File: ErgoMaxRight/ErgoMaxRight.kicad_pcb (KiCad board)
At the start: 2 copper layers, 182.8 x 169.2 mm, 103 parts, among them J1 PJ-320A, K1 F12, K10 8 *, K11 7 &, K12 6 ^, K13 KEYSW, K14 KEYSW, K15 P, K16 O, K17 I, K18 U, K19 Y, K2 F11, K20 KEYSW, K21 KEYSW, K22 ; :, K23 L, K24 K, K25 J, K26 H, K27 KEYSW, K28 KEYSW, K29 KEYSW, K3 F10, K30 / ?, K31 . >, K32 , <, K33 M, K34 N, K35 KEYSW, K36 KEYSW, K37 KEYSW, K38 KEYSW, K39 KEYSW, K4 F9, K40 KEYSW, K41 KEYSW, K42 KEYSW, K43 KEYSW, K44 KEYSW, K5 F8, K6 F7, K7 KEYSW, K8 0 ), K9 9 (, U1 ProMicro

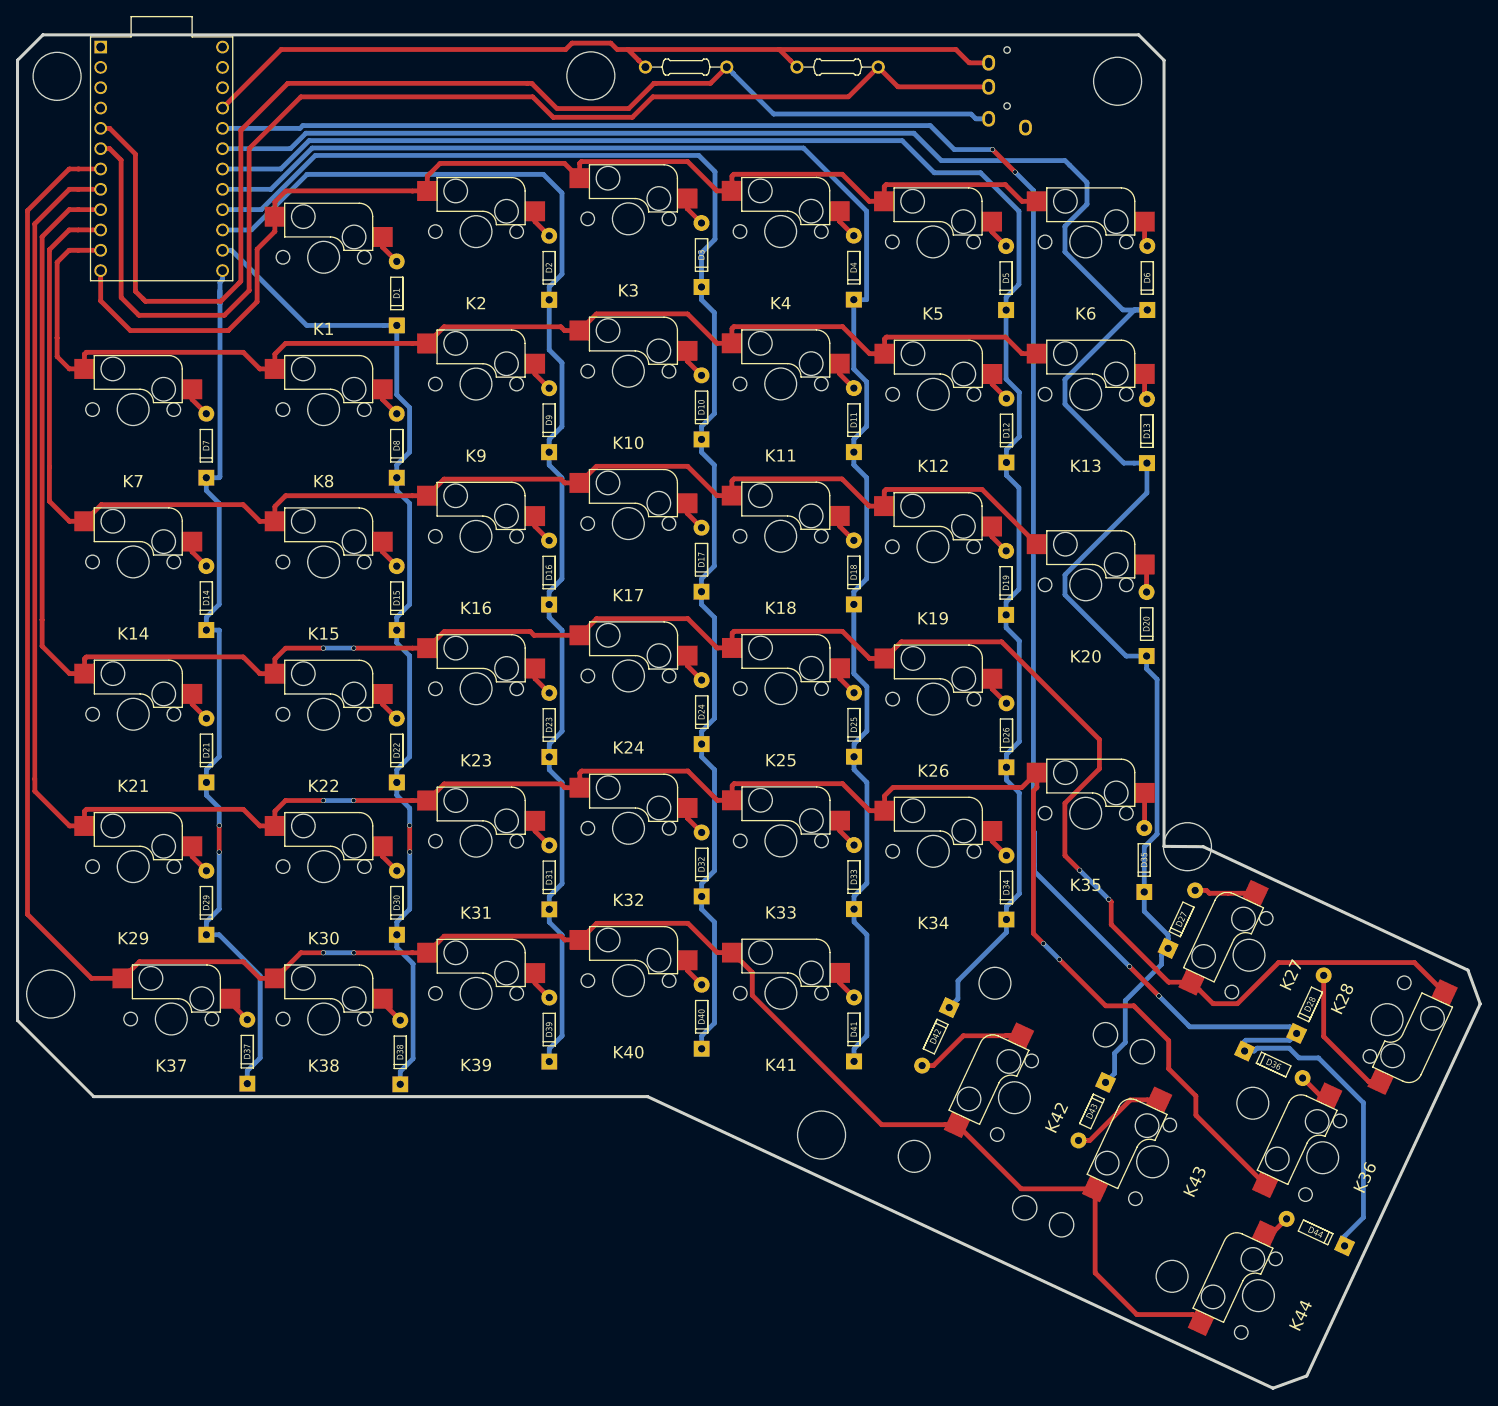
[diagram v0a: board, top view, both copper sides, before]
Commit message: feat: using smd components
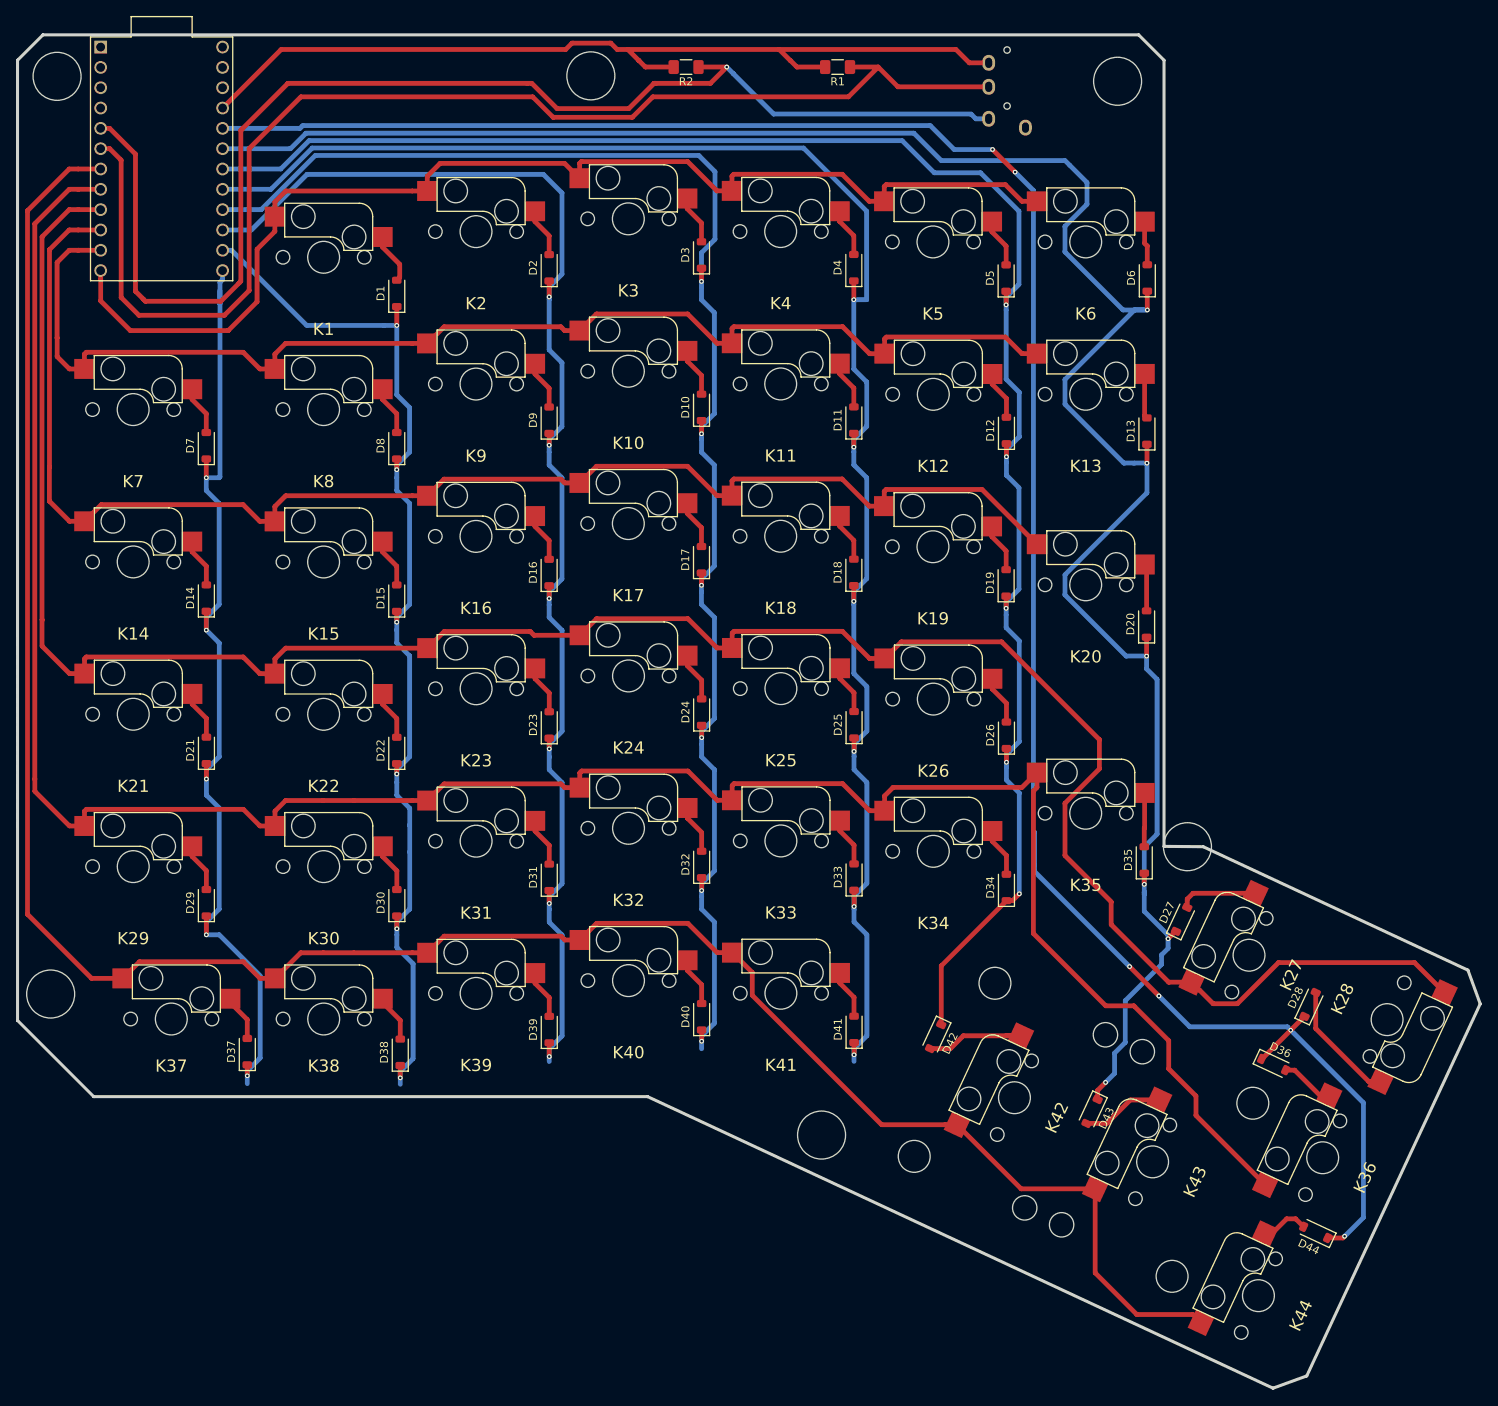
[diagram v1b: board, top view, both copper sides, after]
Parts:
- D1, D10, D11, D12, D13, D14, D15, D16, D17, D18, D19, D2, D20, D21, D22, D23, D24, D25, D26, D27, D28, D29, D3, D30, D31, D32, D33, D34, D35, D36, D37, D38, D39, D4, D40, D41, D42, D43, D44, D5, D6, D7, D8, D9: footprint Keebio-Parts:Diode_Long -> Diode_SMD:D_SOD-123
- R1, R2: footprint Keebio-Parts:Resistor -> Resistor_SMD:R_1206_3216Metric_Pad1.30x1.75mm_HandSolder
- turned D1 to 90 degrees
- turned D10 to 90 degrees
- turned D11 to 90 degrees
- turned D12 to 90 degrees
- turned D13 to 90 degrees
- turned D14 to 90 degrees
- turned D15 to 90 degrees
- turned D16 to 90 degrees
- turned D17 to 90 degrees
- turned D18 to 90 degrees
- turned D19 to 90 degrees
- turned D2 to 90 degrees
- turned D20 to 90 degrees
- turned D21 to 90 degrees
- turned D22 to 90 degrees
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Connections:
- U1 pad 1: Net-(U1-Pad1) -> unconnected-(U1-TX-Pad1)
- U1 pad 2: Net-(U1-Pad2) -> unconnected-(U1-RX-Pad2)
- U1 pad 22: Net-(U1-Pad22) -> unconnected-(U1-RST-Pad22)
- U1 pad 24: Net-(U1-Pad24) -> unconnected-(U1-RAW-Pad24)
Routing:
- net /Col6: track 258.2 -> 270.5 mm, vias 0 -> 6
- net /Col4: track 200.5 -> 211.7 mm, vias 0 -> 6
- net /Col2: track 162.2 -> 171.9 mm, vias 0 -> 6
- net /Col5: track 213.2 -> 222.7 mm, vias 0 -> 5
- net /Col0: track 114.4 -> 123.8 mm, vias 2 -> 5
- net /Col3: track 182.2 -> 191.6 mm, vias 0 -> 6
- net /Col1: track 128.5 -> 136.8 mm, vias 2 -> 6
- net VCC: track 106.4 -> 113.4 mm
- net /Col7: track 276.0 -> 270.6 mm, vias 4 -> 6
- net SCL: track 156.1 -> 159.6 mm
- net SDA: track 158.8 -> 162.3 mm, vias 0 -> 1
- net Net-(D36-A): track 4.23 -> 6.78 mm
- net Net-(D44-A): track 3.48 -> 6.02 mm
- net Net-(D37-A): track 3.51 -> 5.86 mm
- net Net-(D8-A): track 3.80 -> 6.15 mm
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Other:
- copper layers 2 -> 4
- net class Default removed
- rule pad_to_mask_clearance: 0.051 -> 0

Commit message: feat: final version for produccion
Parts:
- moved D35 3.24 mm to (247.9, 139.0)
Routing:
- net /Col6: track 270.5 -> 274.3 mm
- net Net-(D35-A): track 6.75 -> 9.30 mm
- net /Row3: vias 0 -> 2
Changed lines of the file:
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@@
       (plot_on_all_layers_selection 0x0000000_00000000)
       (disableapertmacros false)
-      (usegerberextensions false)
+      (usegerberextensions true)
       (usegerberattributes false)
       (usegerberadvancedattributes false)
@@
       (psa4output false)
       (plotreference true)
-      (plotvalue true)
+      (plotvalue false)
       (plotinvisibletext false)
       (sketchpadsonfab false)
-      (subtractmaskfromsilk false)
+      (subtractmaskfromsilk true)
       (outputformat 1)
       (mirror false)
@@
   )
   (footprint "Diode_SMD:D_SOD-123" (layer "F.Cu")
-    (at 251.18 138.99 90)
+    (at 247.94 138.98 90)
     (descr "SOD-123")
     (tags "SOD-123")
@@
     (fp_line (start 1.6 0.8) (end -1.6 0.8)
       (stroke (width 0.1) (type solid)) (layer "F.Fab"))
-    (pad "1" smd roundrect (at -1.55 0 180) (size 1.3 1.75) (layers "F.Cu" "F.Paste" "F.Mask") (roundrect_rratio 0.192308)
+    (pad "1" smd roundrect (at -1.55 0 180) (size 1.3 1.75) (layers "F.Cu" "F.Paste" "F.Mask") (roundrect_rratio 0.1923076923)
       (net 17 "SCL") (pintype "passive"))
-    (pad "2" smd roundrect (at 1.55 0 180) (size 1.3 1.75) (layers "F.Cu" "F.Paste" "F.Mask") (roundrect_rratio 0.192308)
+    (pad "2" smd roundrect (at 1.55 0 180) (size 1.3 1.75) (layers "F.Cu" "F.Paste" "F.Mask") (roundrect_rratio 0.1923076923)
       (net 15 "VCC") (pintype "passive"))
     (model "${KICAD6_3DMODEL_DIR}/Resistor_SMD.3dshapes/R_1206_3216Metric.wrl"
@@
     (fp_line (start 1.6 0.8) (end -1.6 0.8)
       (stroke (width 0.1) (type solid)) (layer "F.Fab"))
-    (pad "1" smd roundrect (at -1.55 0 180) (size 1.3 1.75) (layers "F.Cu" "F.Paste" "F.Mask") (roundrect_rratio 0.192308)
+    (pad "1" smd roundrect (at -1.55 0 180) (size 1.3 1.75) (layers "F.Cu" "F.Paste" "F.Mask") (roundrect_rratio 0.1923076923)
       (net 16 "SDA") (pintype "passive"))
-    (pad "2" smd roundrect (at 1.55 0 180) (size 1.3 1.75) (layers "F.Cu" "F.Paste" "F.Mask") (roundrect_rratio 0.192308)
+    (pad "2" smd roundrect (at 1.55 0 180) (size 1.3 1.75) (layers "F.Cu" "F.Paste" "F.Mask") (roundrect_rratio 0.1923076923)
       (net 15 "VCC") (pintype "passive"))
     (model "${KICAD6_3DMODEL_DIR}/Resistor_SMD.3dshapes/R_1206_3216Metric.wrl"
@@
   (segment (start 245.35012 167.791762) (end 246.343273 166.798609) (width 0.6) (layer "F.Cu") (net 6))
   (segment (start 251.51334 87.02956) (end 251.51334 89.37956) (width 0.6) (layer "F.Cu") (net 6))
+  (segment (start 247.94 141.21) (end 251.18 144.45) (width 0.6) (layer "F.Cu") (net 6))
   (segment (start 251.55906 67.88558) (end 251.55906 70.23558) (width 0.6) (layer "F.Cu") (net 6))
   (segment (start 251.4727 111.15194) (end 251.4727 113.50194) (width 0.6) (layer "F.Cu") (net 6))
-  (segment (start 251.18 140.64) (end 251.18 142.03) (width 0.6) (layer "F.Cu") (net 6))
   (segment (start 245.35012 168.928432) (end 245.35012 167.791762) (width 0.6) (layer "F.Cu") (net 6))
+  (segment (start 247.94 140.63) (end 247.94 141.21) (width 0.6) (layer "F.Cu") (net 6))
   (segment (start 255.087633 147.911168) (end 254.161187 148.837614) (width 0.6) (layer "F.Cu") (net 6))
   (segment (start 255.15434 147.911168) (end 255.087633 147.911168) (width 0.6) (layer "F.Cu") (net 6))
   (via (at 246.343273 166.798609) (size 0.6) (drill 0.3) (layers "F.Cu" "B.Cu") (net 6))
   (via (at 251.4727 113.50194) (size 0.6) (drill 0.3) (layers "F.Cu" "B.Cu") (net 6))
-  (via (at 251.18 142.03) (size 0.6) (drill 0.3) (layers "F.Cu" "B.Cu") (net 6))
+  (via (at 251.18 144.45) (size 0.6) (drill 0.3) (layers "F.Cu" "B.Cu") (net 6))
   (via (at 254.161187 148.837614) (size 0.6) (drill 0.3) (layers "F.Cu" "B.Cu") (net 6))
   (via (at 251.51334 89.37956) (size 0.6) (drill 0.3) (layers "F.Cu" "B.Cu") (net 6))
@@
   (segment (start 143.8534 112.51024) (end 161.57 112.51024) (width 0.6) (layer "F.Cu") (net 12))
   (segment (start 180.62 110.90724) (end 180.645 110.90724) (width 0.6) (layer "F.Cu") (net 12))
+  (segment (start 239.01 117.38) (end 239.01 117.42) (width 0.6) (layer "F.Cu") (net 12))
   (segment (start 174.430439 110.430439) (end 174.90724 110.90724) (width 0.6) (layer "F.Cu") (net 12))
+  (segment (start 233.348939 111.721039) (end 233.351039 111.721039) (width 0.6) (layer "F.Cu") (net 12))
   (segment (start 142.5116 115.70204) (end 142.5116 113.85204) (width 0.6) (layer "F.Cu") (net 12))
   (segment (start 216.845 113.80084) (end 218.72 113.80084) (width 0.6) (layer "F.Cu") (net 12))
@@
   (segment (start 288.712471 155.573879) (end 284.95422 151.815628) (width 0.6) (layer "F.Cu") (net 12))
   (segment (start 163.674801 110.430439) (end 161.595 112.51024) (width 0.6) (layer "F.Cu") (net 12))
+  (segment (start 233.351039 111.721039) (end 239.01 117.38) (width 0.6) (layer "F.Cu") (net 12))
   (segment (start 118.7154 113.84384) (end 118.945201 113.614039) (width 0.6) (layer "F.Cu") (net 12))
-  (segment (start 245.57482 123.94692) (end 233.348939 111.721039) (width 0.6) (layer "F.Cu") (net 12))
+  (via (at 245.57482 123.94692) (size 0.6) (drill 0.3) (layers "F.Cu" "B.Cu") (net 12))
+  (via (at 239.01 117.42) (size 0.6) (drill 0.3) (layers "F.Cu" "B.Cu") (net 12))
+  (segment (start 245.53692 123.94692) (end 245.57482 123.94692) (width 0.6) (layer "B.Cu") (net 12))
+  (segment (start 239.01 117.42) (end 245.53692 123.94692) (width 0.6) (layer "B.Cu") (net 12))
   (segment (start 152.3619 131.56) (end 159.695 131.56) (width 0.6) (layer "F.Cu") (net 13))
   (segment (start 197.795 131.53) (end 199.67 131.53) (width 0.6) (layer "F.Cu") (net 13))
@@
   (segment (start 232.17 136.645165) (end 233.954161 138.429326) (width 0.6) (layer "F.Cu") (net 52))
   (segment (start 232.17 135.37) (end 232.17 136.645165) (width 0.6) (layer "F.Cu") (net 52))
-  (segment (start 251.22 134.95) (end 251.18 134.99) (width 0.6) (layer "F.Cu") (net 53))
-  (segment (start 251.18 134.99) (end 251.18 137.34) (width 0.6) (layer "F.Cu") (net 53))
-  (segment (start 251.22 130.61) (end 251.22 134.95) (width 0.6) (layer "F.Cu") (net 53))
+  (segment (start 251.22 136.13) (end 251.22 130.61) (width 0.6) (layer "F.Cu") (net 53))
+  (segment (start 250.02 137.33) (end 251.22 136.13) (width 0.6) (layer "F.Cu") (net 53))
+  (segment (start 247.94 137.33) (end 250.02 137.33) (width 0.6) (layer "F.Cu") (net 53))
   (segment (start 268.845648 165.25884) (end 269.982318 165.25884) (width 0.6) (layer "F.Cu") (net 54))
   (segment (start 273.191158 168.46768) (end 274.292254 168.46768) (width 0.6) (layer "F.Cu") (net 54))

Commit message: updated for jlcpcb available components
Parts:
- K13: value KEYSW -> K13
- K14: value KEYSW -> K14
- K20: value KEYSW -> K20
- K21: value KEYSW -> K21
- K27: value KEYSW -> K27
- K28: value KEYSW -> K28
- K29: value KEYSW -> K29
- K35: value KEYSW -> K35
- K36: value KEYSW -> K36
- K37: value KEYSW -> K37
- K38: value KEYSW -> K38
- K39: value KEYSW -> K39
- K40: value KEYSW -> K40
- K41: value KEYSW -> K41
- K42: value KEYSW -> K42
- K43: value KEYSW -> K43
- K44: value KEYSW -> K44
- K7: value KEYSW -> K7
